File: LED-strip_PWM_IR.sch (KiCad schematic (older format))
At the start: 17 parts, among them IC1 ATtiny85, P1 CONN_2, P2 CONN_2, Q1 8MHz, T1 IRLR2905_DPAK, U1 TSOP38238, U2 MCP1804-SOT23-5

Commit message: Switched to REV. 202 of atmel.lib
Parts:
- removed IC1: ATtiny85, DIP8, symbol ATTINY85-P
- added IC1: ATTINY85-S, SO8-200, symbol ATTINY85-S
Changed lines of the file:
@@
-EESchema Schematic File Version 2  date Thu 10 Jan 2013 12:08:27 AM CET
+EESchema Schematic File Version 2  date Sun 27 Jan 2013 10:33:05 AM CET
 LIBS:my_parts
 LIBS:power
@@
 LIBS:contrib
 LIBS:valves
-LIBS:atmel_rev110
 LIBS:murata-resonators
 LIBS:LED-strip_PWM_IR-cache
@@
 Sheet 1 1
 Title "LED-strip_PWM_IR"
-Date "9 jan 2013"
+Date "27 jan 2013"
 Rev "0.2"
 Comp "2012 - blog.spitzenpfeil.org"
@@
 $EndComp
 $Comp
-L ATTINY85-P IC1
-U 1 1 4F6EC673
-P 1800 1050
-F 0 "IC1" H 1900 1100 60  0000 C CNN
-F 1 "ATtiny85" H 3800 1100 60  0000 C CNN
-F 2 "DIP8" H 1900 300 60  0001 C CNN
-	1    1800 1050
-	1    0    0    -1
-$EndComp
-$Comp
 L PWR_FLAG #FLG010
 U 1 1 50B1E380
@@
 	2950 4000 2950 4050
 Connection ~ 2950 4000
+$Comp
+L ATTINY85-S IC1
+U 1 1 5104F51F
+P 2950 1400
+F 0 "IC1" H 1900 1800 60  0000 C CNN
+F 1 "ATTINY85-S" H 3800 1000 60  0000 C CNN
+F 2 "SO8-200" H 2050 1000 60  0000 C CNN
+	1    2950 1400
+	1    0    0    -1
+$EndComp
 $EndSCHEMATC

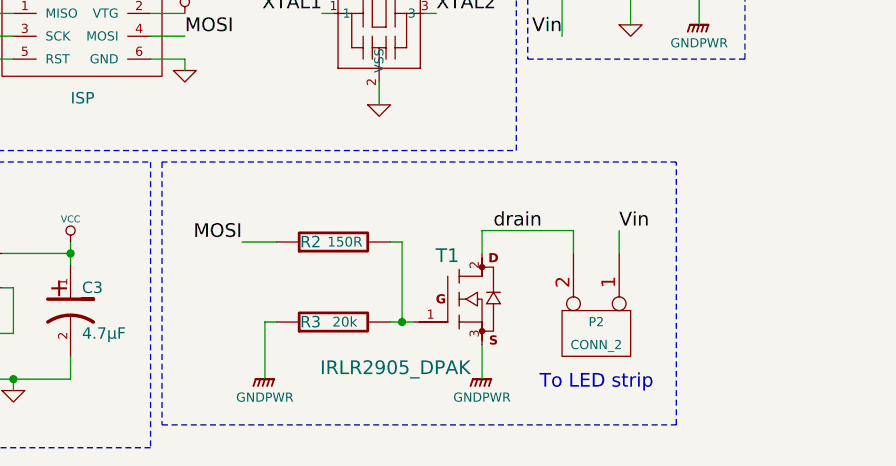
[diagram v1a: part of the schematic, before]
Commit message: Added a protection Schottky-Diode for the MOSFET. Now V0.3
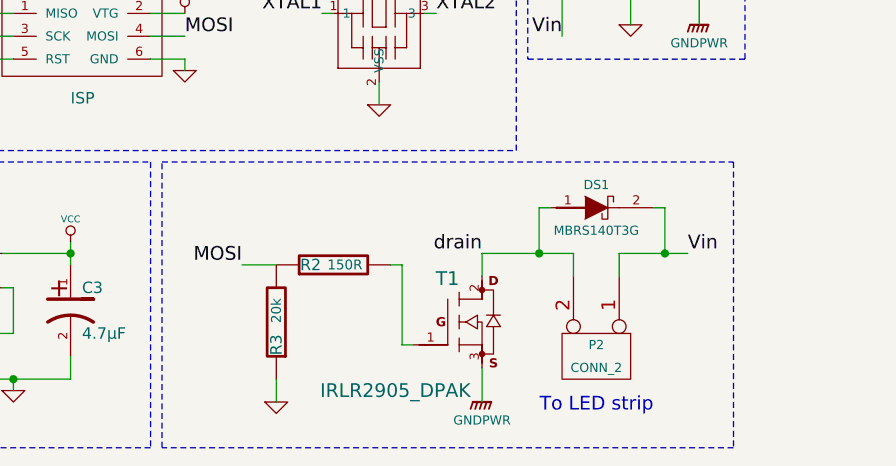
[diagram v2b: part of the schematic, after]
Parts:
- added DS1: MBRS140T3G, ~, symbol DIODESCH
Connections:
- net GND: now also R3.1
- net GNDPWR: no longer R3.1
- net MOSI: now also R3.2
- net Vin: now also DS1.2 (C)
- net drain: now also DS1.1 (A)
- net at R2.2, T1.1 (G): no longer R3.2
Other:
- moved on the sheet: P2, R2, R3, T1
